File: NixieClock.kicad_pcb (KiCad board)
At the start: 2 copper layers, 170 x 132 mm, 174 parts, among them J1 Barrel_Jack, Q1 MPSA42, Q10 MPSA42, Q11 MPSA42, Q12 MPSA42, Q13 KSP92BU, Q14 KSP92BU, Q15 MPSA42, Q16 MPSA42, Q17 MPSA42, Q18 MPSA42, Q19 KSP92BU, Q2 MPSA42, Q20 KSP92BU, Q21 MPSA42, Q22 MPSA42, Q23 KSP92BU, Q24 KSP92BU, Q25 KSP2907A, Q26 IRF644, Q3 MPSA42, Q4 MPSA42, Q5 MPSA42, Q6 MPSA42, Q7 MPSA42, Q8 MPSA42, Q9 MPSA42, SW1 PB400EEQX, SW2 SW_Push, SW3 SW_Push, SW4 SW_Push, U1 L7805, U10 74LS160, U11 74LS160, U12 74LS160, U13 74LS160, U14 74LS160, U15 74HC4060, U16 4028, U17 74LS151, U18 74LS151, U19 74LS151, U2 MC34063AP, U20 4028, U21 74LS151, U3 74LS14, U4 74LS109, U5 74LS10, U6 74LS08, U7 74LS393, U8 74LS20, U9 74LS160, Y1 32.768 kHz - 12.5pF

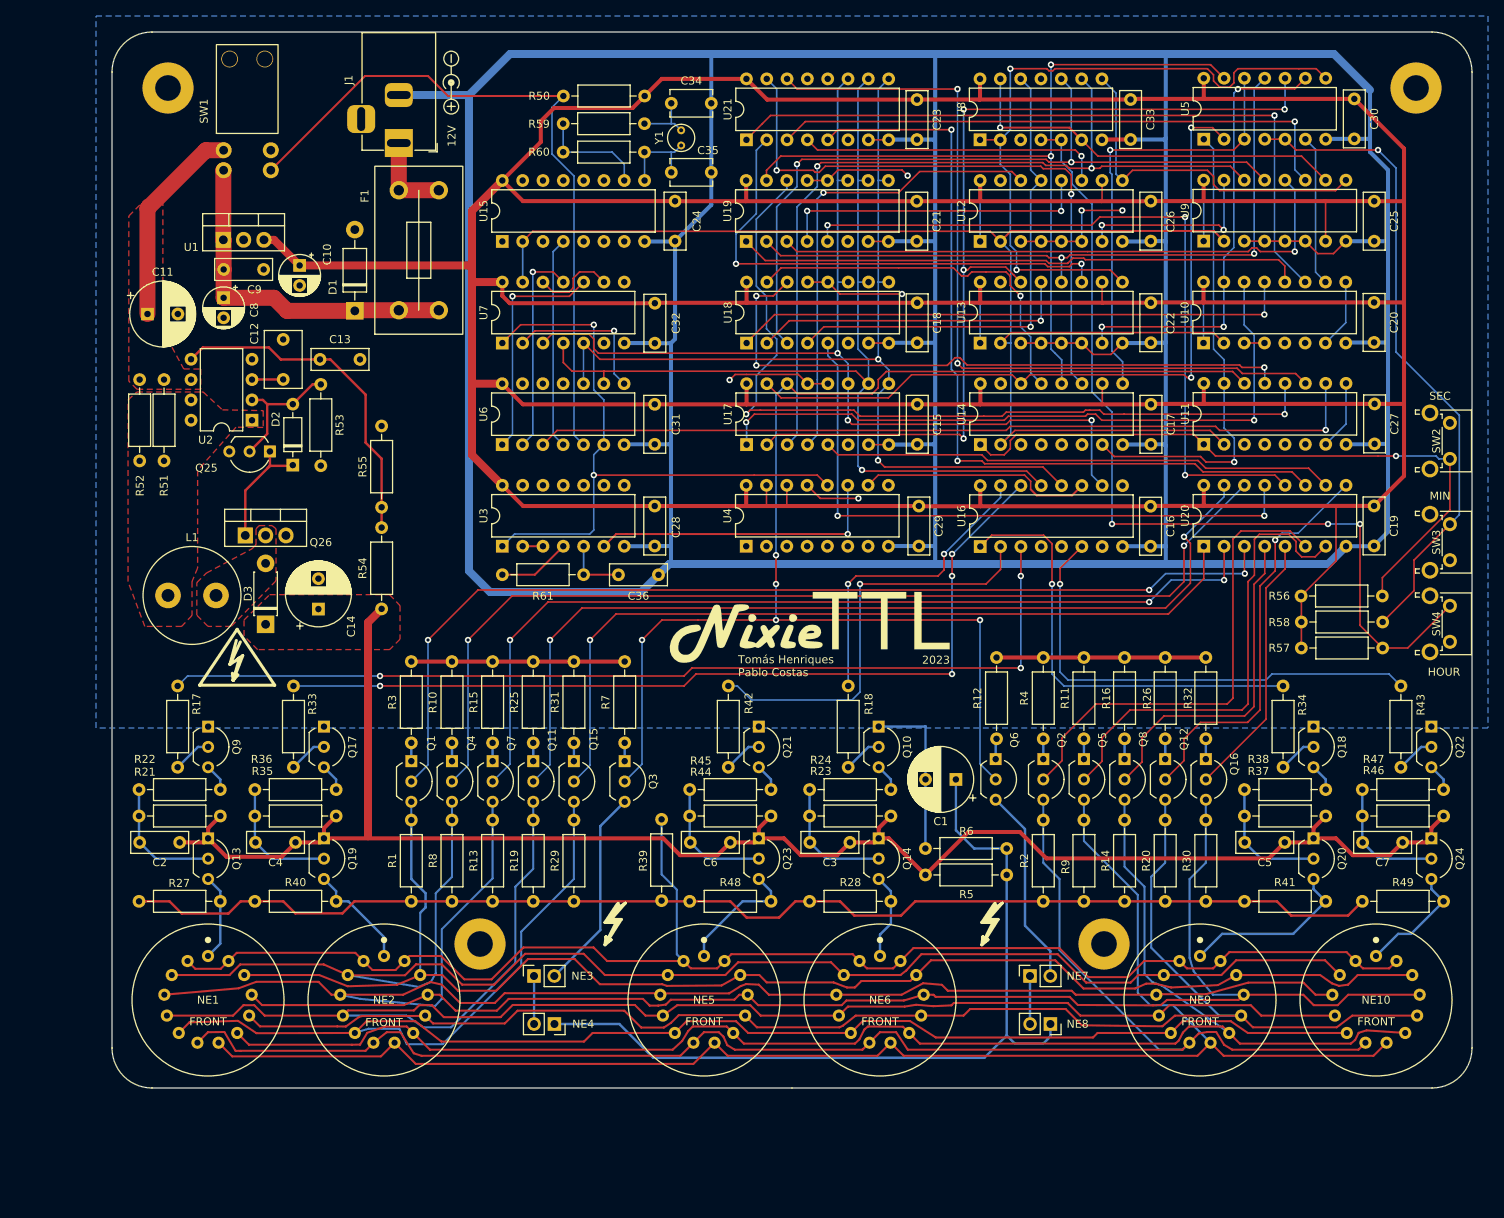
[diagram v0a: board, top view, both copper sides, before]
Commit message: Pablo's review, several changes:
Schematic:
- Overall aesthetics
- Added PWR_FLAG to remove ERC errors.
Layout:
- Overall component alignment
- Removed some loops and unnecessary vias.
- Cleaned up vias without ends.
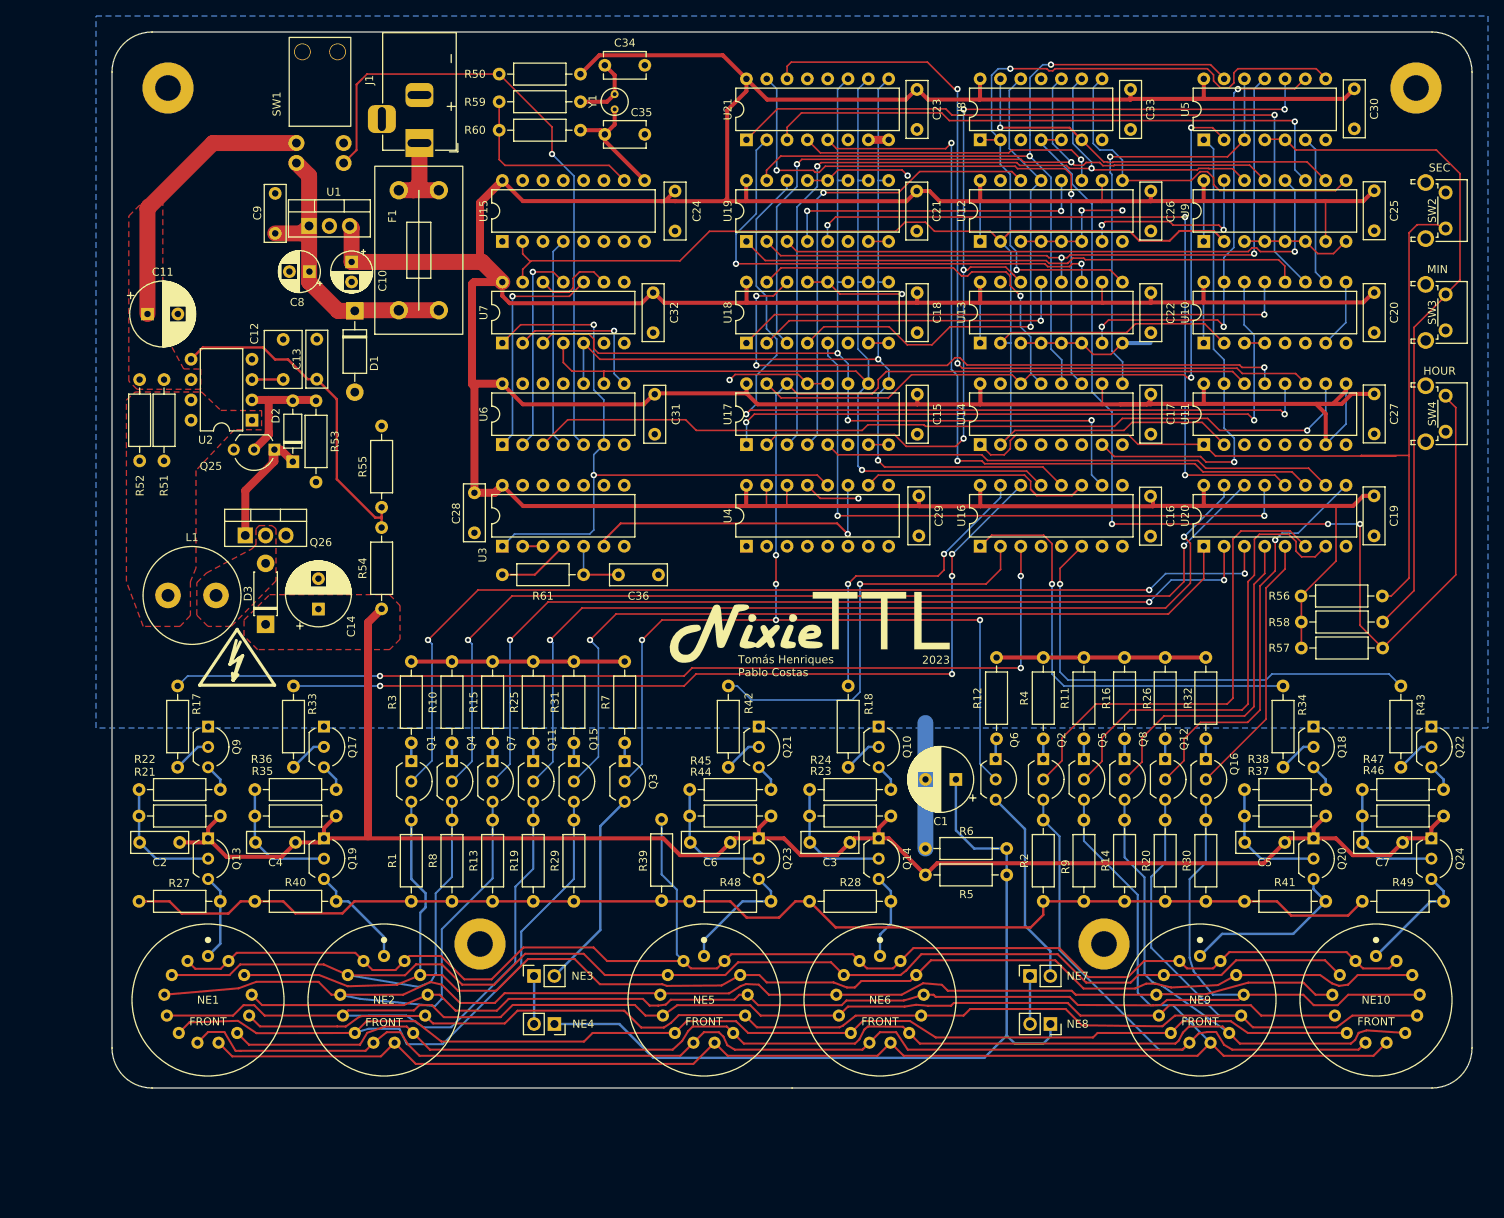
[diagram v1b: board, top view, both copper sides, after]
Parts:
- removed 12V: Symbol_Barrel_Polarity, Symbol:Symbol_Barrel_Polarity
- removed the REF** at (162.0, 141.1)
- removed the REF** at (209.1, 141.1)
- R51, R52: value 1.69 -> 1R69
- moved SW2 28.8 mm to (266.7, 49.1)
- moved SW3 28.7 mm to (266.7, 61.8)
- moved SW4 26.3 mm to (266.7, 74.5)
- moved C28 22.6 mm to (145.3, 86.6)
- moved C8 11.2 mm to (124.7, 59.0), turned to 180 degrees
- moved U1 10.9 mm to (124.6, 53.2)
- moved C34 9.57 mm to (161.6, 33.2)
- moved C35 9.57 mm to (161.6, 41.8)
- moved Y1 9.46 mm to (162.8, 38.7)
- moved SW1 9.14 mm to (128.9, 45.4)
- moved R50 8.48 mm to (148.4, 34.3)
- moved R60 8.46 mm to (148.4, 41.3)
- moved R59 8.46 mm to (158.6, 37.7)
- moved C9 7.87 mm to (120.4, 54.2), turned to 90 degrees
- moved C10 6.51 mm to (129.9, 57.7)
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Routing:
- net GND: track 833.0 -> 190.4 mm
- net +5V: track 827.7 -> 791.6 mm
- net Net-(R56-Pad2): track 82.8 -> 114.1 mm, vias 1 -> 0
- net Net-(R57-Pad2): track 111.4 -> 137.5 mm
- net Net-(R59-Pad2): track 13.9 -> 23.9 mm
- net Net-(C11-Pad1): track 25.7 -> 35.2 mm
- net DISP_EN: track 88.3 -> 79.5 mm, vias 0 -> 1
- net Net-(D2-Pad1): track 15.1 -> 21.7 mm
- net +12V: track 43.6 -> 37.9 mm
- net 4Hz: track 180.9 -> 185.6 mm
- net Net-(R58-Pad2): track 81.9 -> 86.1 mm, vias 1 -> 0
- net Net-(C35-Pad1): track 11.0 -> 14.7 mm
- net Net-(D2-Pad2): track 16.7 -> 20.2 mm
- net H_DE_B: track 61.3 -> 64.4 mm
- net HT: track 220.1 -> 217.3 mm
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
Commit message: WIP
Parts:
- removed ? (x2): , 
- removed C5, C7: 10n, Capacitor_THT:C_Rect_L7.0mm_W2.5mm_P5.00mm
- removed NE10, NE9: IN-14, NixieClock:IN-14
- removed NE7, NE8: INS-1, Connector_PinSocket_2.54mm:PinSocket_1x02_P2.54mm_Vertical
- removed Q18, Q22, Q6: MPSA42, Package_TO_SOT_THT:TO-92_Inline_Wide
- removed Q20, Q24: KSP92BU, Package_TO_SOT_THT:TO-92_Inline_Wide
- removed R12: 11k 1%, Resistor_THT:R_Axial_DIN0207_L6.3mm_D2.5mm_P10.16mm_Horizontal
- removed R34, R43, R56: 11k, Resistor_THT:R_Axial_DIN0207_L6.3mm_D2.5mm_P10.16mm_Horizontal
- removed R37, R46: 4k42, Resistor_THT:R_Axial_DIN0207_L6.3mm_D2.5mm_P10.16mm_Horizontal
- removed R38, R41, R47, R49: 220k, Resistor_THT:R_Axial_DIN0207_L6.3mm_D2.5mm_P10.16mm_Horizontal
- removed SW2: SW_Push, Button_Switch_THT:SW_Tactile_SPST_Angled_PTS645Vx83-2LFS
- C1: footprint Capacitor_THT:CP_Radial_D8.0mm_P3.80mm -> Capacitor_SMD:C_1812_4532Metric
- C13, C2, C3, C4, C6: footprint Capacitor_THT:C_Rect_L7.0mm_W2.5mm_P5.00mm -> Capacitor_SMD:C_0805_2012Metric
- C34, C35: footprint Capacitor_THT:C_Disc_D5.1mm_W3.2mm_P5.00mm -> Capacitor_SMD:C_0805_2012Metric
- Q1, Q10, Q11, Q12, Q13, Q14, Q15, Q16, Q17, Q19, Q2, Q21, Q23, Q3, Q4, Q5, Q7, Q8, Q9: footprint Package_TO_SOT_THT:TO-92_Inline_Wide -> Package_TO_SOT_SMD:SOT-23
- R1, R10, R11, R13, R14, R15, R16, R17, R18, R19, R2, R20, R21, R22, R23, R24, R25, R26, R27, R28, R29, R3, R30, R31, R32, R33, R35, R36, R39, R4, R40, R42, R44, R45, R48, R5, R50, R51, R52, R53, R54, R55, R57, R58, R59, R6, R60, R61, R7, R8, R9: footprint Resistor_THT:R_Axial_DIN0207_L6.3mm_D2.5mm_P10.16mm_Horizontal -> Resistor_SMD:R_0805_2012Metric
- moved R4 51.2 mm to (248.9, 156.9), turned to -90 degrees
- moved R31 49.6 mm to (127.2, 156.9)
- moved R6 47.9 mm to (164.4, 124.6), turned to 0 degrees
- moved Q2 47.3 mm to (245.9, 156.9), turned to 180 degrees
- moved Q15 46.0 mm to (130.1, 156.9), turned to 0 degrees
- moved R11 45.3 mm to (248.9, 153.4), turned to -90 degrees
- moved R25 43.8 mm to (127.2, 153.4)
- moved R17 43.5 mm to (147.6, 129.3)
- moved C1 43.1 mm to (162.7, 127.6), turned to 0 degrees
- moved R22 42.6 mm to (145.6, 129.3), turned to -90 degrees
- moved R5 41.9 mm to (161.0, 124.6)
- moved Q5 41.5 mm to (245.9, 153.4), turned to 180 degrees
- moved R58 40.7 mm to (261.2, 64.1), turned to -90 degrees
- moved Q11 40.2 mm to (130.1, 153.4), turned to 0 degrees
- moved R33 40.2 mm to (157.4, 131.0)
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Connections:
- Q1 pad 1: Net-(Q1-Pad1) -> CA0
- Q1 pad 2: CA0 -> Net-(Q1-Pad2)
- Q10 pad 1: GND -> Net-(Q10-Pad1)
- Q10 pad 2: Net-(Q10-Pad2) -> GND
- Q11 pad 1: Net-(Q11-Pad1) -> CA3
- Q11 pad 2: CA3 -> Net-(Q11-Pad2)
- Q12 pad 1: Net-(Q12-Pad1) -> CA8
- Q12 pad 2: CA8 -> Net-(Q12-Pad2)
- Q13 pad 1: HT -> Net-(C2-Pad2)
- Q13 pad 2: Net-(C2-Pad2) -> HT
- Q14 pad 1: HT -> Net-(C3-Pad2)
- Q14 pad 2: Net-(C3-Pad2) -> HT
- Q15 pad 1: Net-(Q15-Pad1) -> CA4
- Q15 pad 2: CA4 -> Net-(Q15-Pad2)
- Q16 pad 1: Net-(Q16-Pad1) -> CA9
- Q16 pad 2: CA9 -> Net-(Q16-Pad2)
- Q17 pad 1: GND -> Net-(Q17-Pad1)
- Q17 pad 2: Net-(Q17-Pad2) -> GND
- Q19 pad 1: HT -> Net-(C4-Pad2)
- Q19 pad 2: Net-(C4-Pad2) -> HT
- Q2 pad 1: Net-(Q2-Pad1) -> CA5
- Q2 pad 2: CA5 -> Net-(Q2-Pad2)
- Q21 pad 1: GND -> Net-(Q21-Pad1)
- Q21 pad 2: Net-(Q21-Pad2) -> GND
- Q23 pad 1: HT -> Net-(C6-Pad2)
- Q23 pad 2: Net-(C6-Pad2) -> HT
- Q3 pad 1: Net-(Q3-Pad1) -> S_UN_A
- Q3 pad 2: S_UN_A -> Net-(Q3-Pad2)
- Q4 pad 1: Net-(Q4-Pad1) -> CA1
- Q4 pad 2: CA1 -> Net-(Q4-Pad2)
- Q5 pad 1: Net-(Q5-Pad1) -> CA6
- Q5 pad 2: CA6 -> Net-(Q5-Pad2)
- Q7 pad 1: Net-(Q7-Pad1) -> CA2
- Q7 pad 2: CA2 -> Net-(Q7-Pad2)
- Q8 pad 1: Net-(Q8-Pad1) -> CA7
- Q8 pad 2: CA7 -> Net-(Q8-Pad2)
- Q9 pad 1: GND -> Net-(Q9-Pad1)
- Q9 pad 2: Net-(Q9-Pad2) -> GND
- R10 pad 1: Net-(Q4-Pad1) -> Net-(Q4-Pad2)
- R11 pad 1: Net-(Q5-Pad1) -> Net-(Q5-Pad2)
- R15 pad 1: Net-(Q7-Pad1) -> Net-(Q7-Pad2)
- R16 pad 1: Net-(Q8-Pad1) -> Net-(Q8-Pad2)
- R17 pad 2: Net-(Q9-Pad2) -> Net-(Q9-Pad1)
- R18 pad 2: Net-(Q10-Pad2) -> Net-(Q10-Pad1)
- R25 pad 1: Net-(Q11-Pad1) -> Net-(Q11-Pad2)
- R26 pad 1: Net-(Q12-Pad1) -> Net-(Q12-Pad2)
- R3 pad 1: Net-(Q1-Pad1) -> Net-(Q1-Pad2)
- R31 pad 1: Net-(Q15-Pad1) -> Net-(Q15-Pad2)
- R32 pad 1: Net-(Q16-Pad1) -> Net-(Q16-Pad2)
- R33 pad 2: Net-(Q17-Pad2) -> Net-(Q17-Pad1)
- R4 pad 1: Net-(Q2-Pad1) -> Net-(Q2-Pad2)
- R42 pad 2: Net-(Q21-Pad2) -> Net-(Q21-Pad1)
- R7 pad 1: Net-(Q3-Pad1) -> Net-(Q3-Pad2)
- U11 pad 1: Net-(R56-Pad2) -> +5V
- U14 pad 1: Net-(R56-Pad2) -> +5V
- U16 pad 1: AN5 -> unconnected-(U16-Pad1)
- U16 pad 6: AN6 -> unconnected-(U16-Pad6)
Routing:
- net HT: track 217.3 -> 11.3 mm
- net COM: track 162.3 -> 0.00 mm
- net Net-(R56-Pad2): track 114.1 -> 0.00 mm
- net AN2: track 110.1 -> 0.00 mm, vias 4 -> 0
- net K4: track 202.0 -> 101.6 mm
- net K3: track 199.2 -> 99.8 mm
- net CS_A: track 104.3 -> 6.27 mm
- net K2: track 191.8 -> 98.4 mm
- net K1: track 191.1 -> 101.7 mm
- net K5: track 198.2 -> 109.1 mm, vias 0 -> 1
- net K6: track 192.3 -> 104.5 mm
- net KDP: track 184.1 -> 97.3 mm
- net K7: track 191.5 -> 105.6 mm
- net K8: track 187.4 -> 103.1 mm
- net K9: track 182.1 -> 103.3 mm
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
